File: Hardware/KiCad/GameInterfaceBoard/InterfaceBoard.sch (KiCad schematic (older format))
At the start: 23 parts, among them J1 CONN_11LOCK, J2 CONN_07LOCK

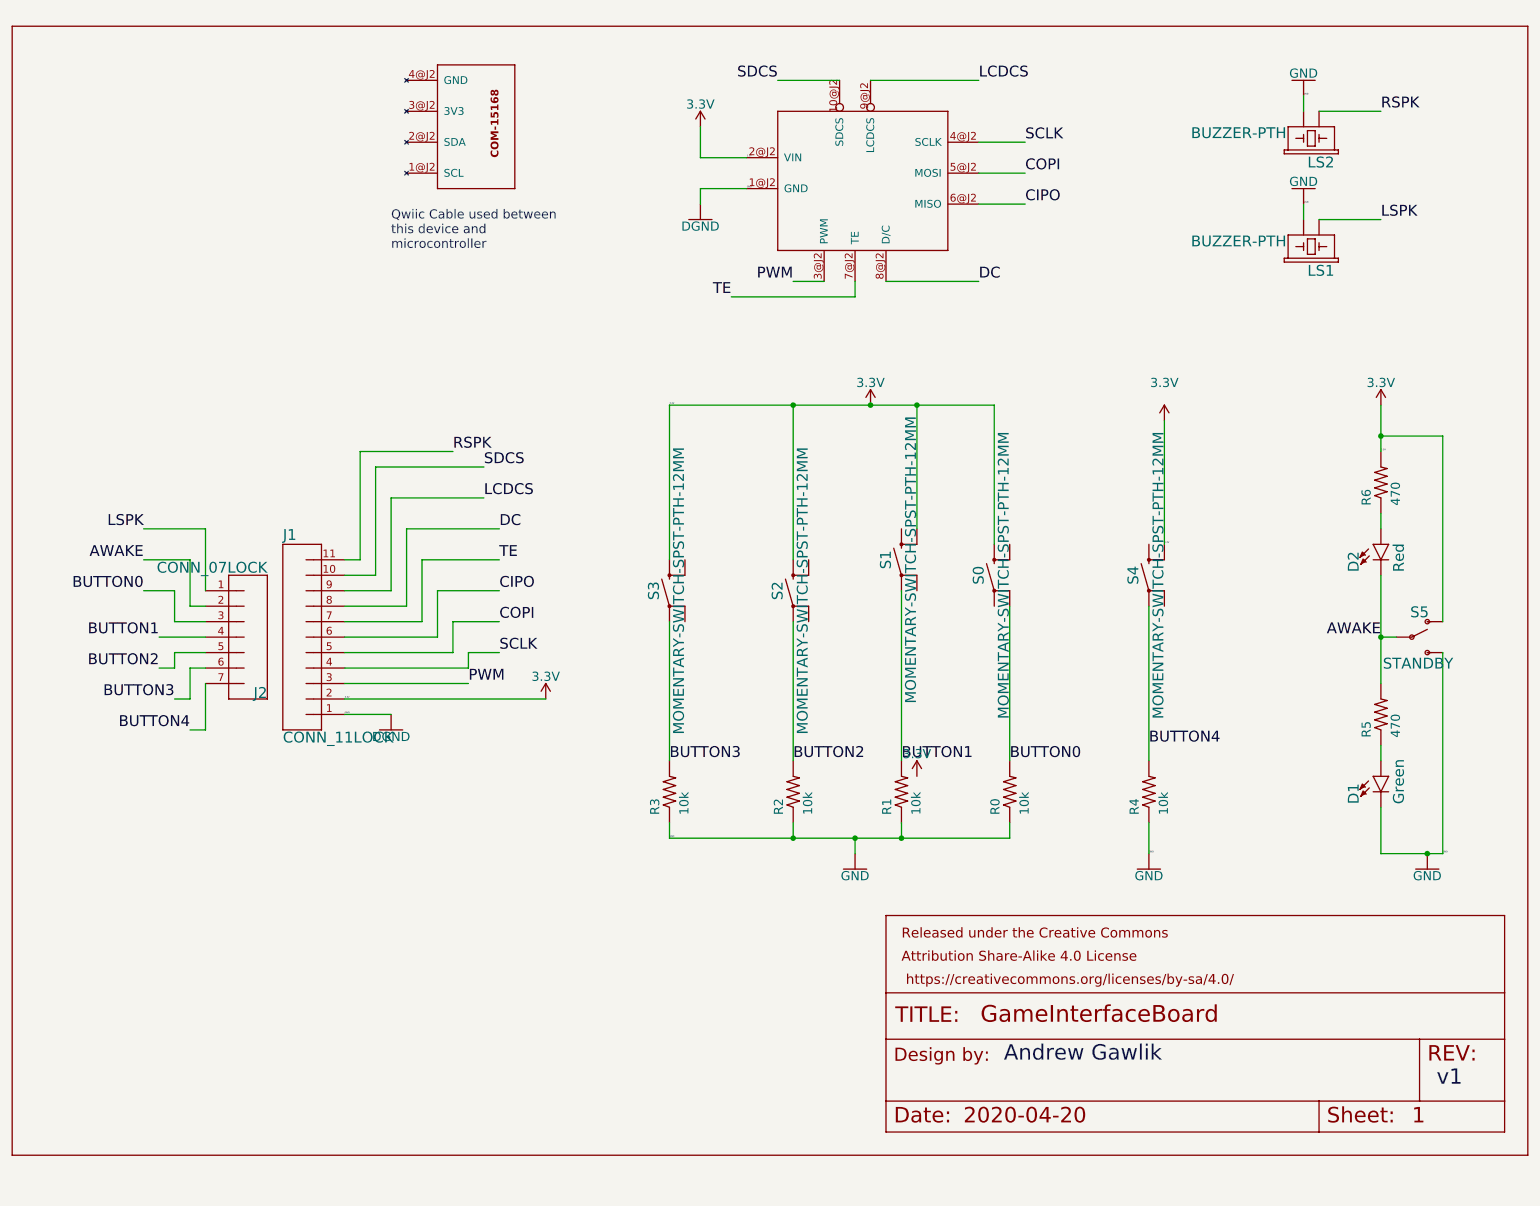
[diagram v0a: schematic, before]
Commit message: Added drill holes for issue #2
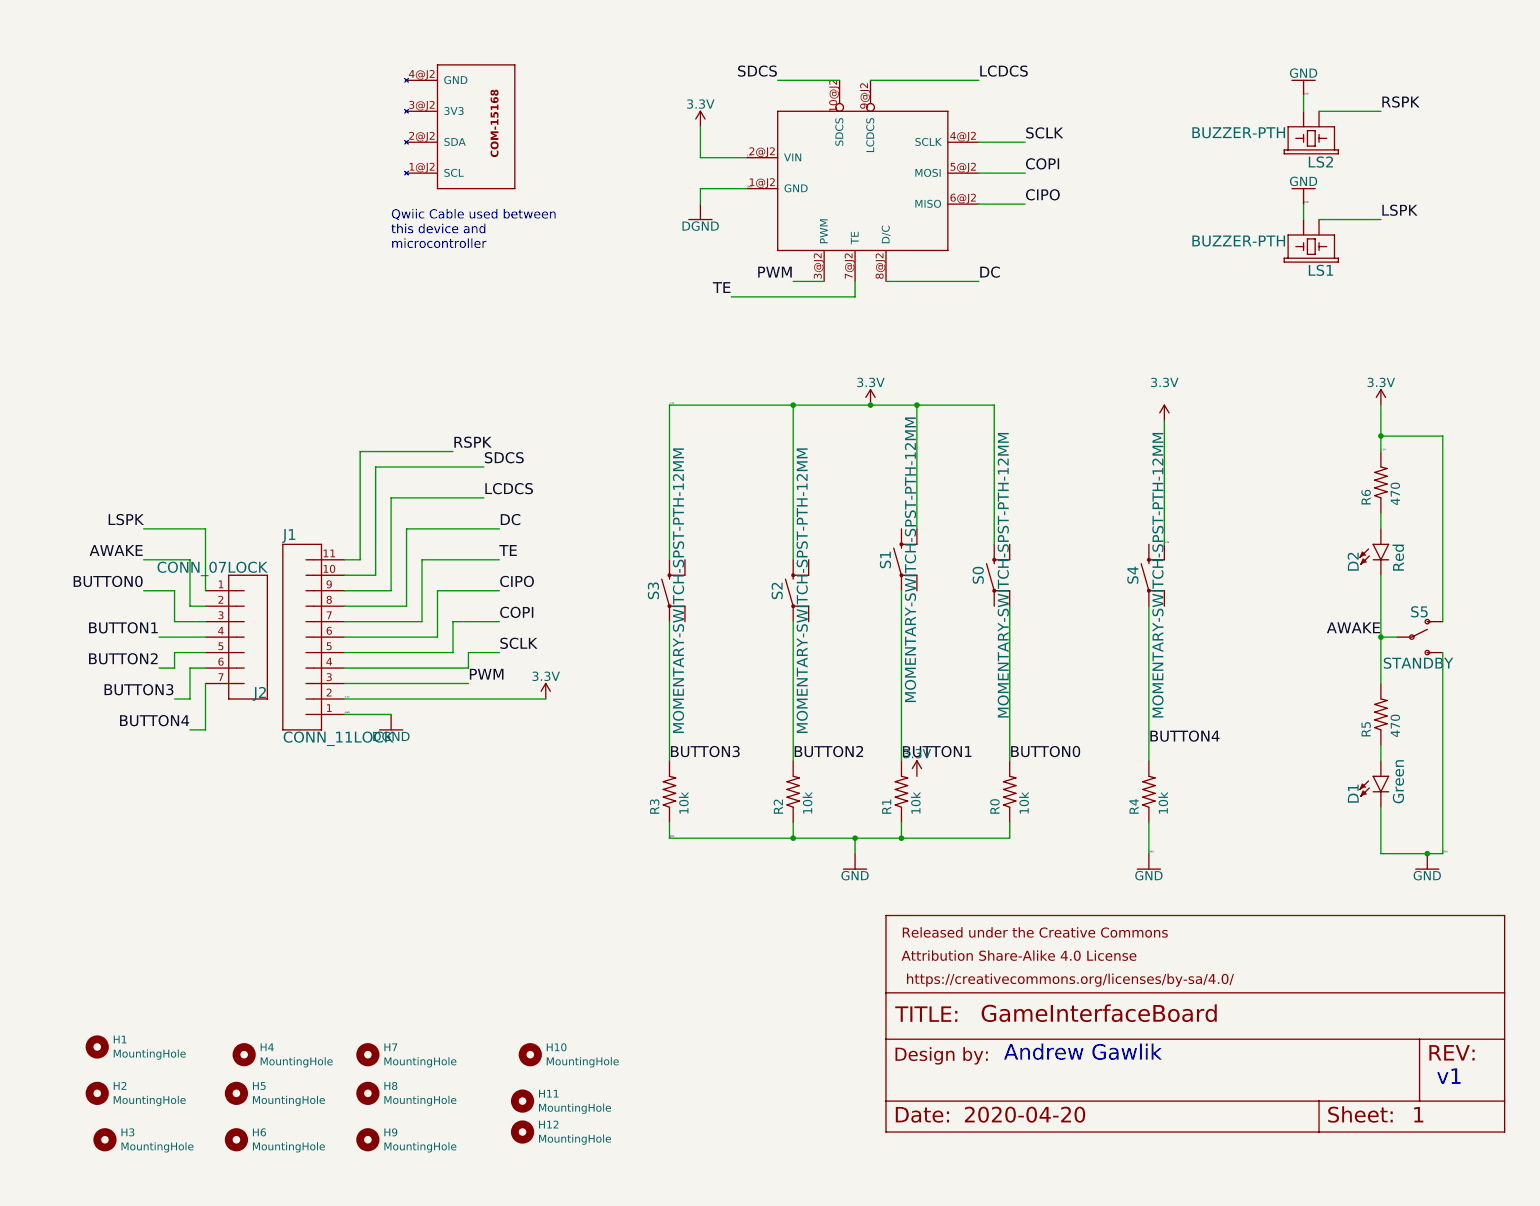
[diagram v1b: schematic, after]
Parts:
- removed FRAME2: FRAME-LETTER, InterfaceBoard:CREATIVE_COMMONS, symbol InterfaceBoard-eagle-import:FRAME-LETTER
- added H1, H10, H11, H12, H2, H3, H4, H5, H6, H7, H8, H9: MountingHole, MountingHole_3mm, symbol Mechanical:MountingHole
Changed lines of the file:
@@
 Text Notes 3700 2300 0    59   ~ 0
 Qwiic Cable used between\nthis device and\nmicrocontroller
-$Comp
-L InterfaceBoard-eagle-import:FRAME-LETTER FRAME2
-U 1 1 608402A7
-P 1250 8150
-F 0 "FRAME2" H 1250 8150 50  0001 C CNN
-F 1 "FRAME-LETTER" H 1250 8150 50  0001 C CNN
-F 2 "InterfaceBoard:CREATIVE_COMMONS" H 1250 8150 50  0001 C CNN
-F 3 "" H 1250 8150 50  0001 C CNN
-	1    1250 8150
-	1    0    0    -1
-$EndComp
 $Bitmap
 Pos 10450 6850
@@
 EndData
 $EndBitmap
+$Comp
+L Mechanical:MountingHole H4
+U 1 1 60808813
+P 2750 7500
+F 0 "H4" H 2850 7546 50  0000 L CNN
+F 1 "MountingHole" H 2850 7455 50  0000 L CNN
+F 2 "MountingHole_3mm" H 2750 7500 50  0001 C CNN
+F 3 "~" H 2750 7500 50  0001 C CNN
+	1    2750 7500
+	1    0    0    -1
+$EndComp
+$Comp
+L Mechanical:MountingHole H1
+U 1 1 6080D86C
+P 1800 7450
+F 0 "H1" H 1900 7496 50  0000 L CNN
+F 1 "MountingHole" H 1900 7405 50  0000 L CNN
+F 2 "MountingHole_3mm" H 1800 7450 50  0001 C CNN
+F 3 "~" H 1800 7450 50  0001 C CNN
+	1    1800 7450
+	1    0    0    -1
+$EndComp
+$Comp
+L Mechanical:MountingHole H7
+U 1 1 6081064F
+P 3550 7500
+F 0 "H7" H 3650 7546 50  0000 L CNN
+F 1 "MountingHole" H 3650 7455 50  0000 L CNN
+F 2 "MountingHole_3mm" H 3550 7500 50  0001 C CNN
+F 3 "~" H 3550 7500 50  0001 C CNN
+	1    3550 7500
+	1    0    0    -1
+$EndComp
+$Comp
+L Mechanical:MountingHole H8
+U 1 1 60810B66
+P 3550 7750
+F 0 "H8" H 3650 7796 50  0000 L CNN
+F 1 "MountingHole" H 3650 7705 50  0000 L CNN
+F 2 "MountingHole_3mm" H 3550 7750 50  0001 C CNN
+F 3 "~" H 3550 7750 50  0001 C CNN
+	1    3550 7750
+	1    0    0    -1
+$EndComp
+$Comp
+L Mechanical:MountingHole H3
+U 1 1 608113E1
+P 1850 8050
+F 0 "H3" H 1950 8096 50  0000 L CNN
+F 1 "MountingHole" H 1950 8005 50  0000 L CNN
+F 2 "MountingHole_3mm" H 1850 8050 50  0001 C CNN
+F 3 "~" H 1850 8050 50  0001 C CNN
+	1    1850 8050
+	1    0    0    -1
+$EndComp
+$Comp
+L Mechanical:MountingHole H6
+U 1 1 60811785
+P 2700 8050
+F 0 "H6" H 2800 8096 50  0000 L CNN
+F 1 "MountingHole" H 2800 8005 50  0000 L CNN
+F 2 "MountingHole_3mm" H 2700 8050 50  0001 C CNN
+F 3 "~" H 2700 8050 50  0001 C CNN
+	1    2700 8050
+	1    0    0    -1
+$EndComp
+$Comp
+L Mechanical:MountingHole H10
+U 1 1 60811E6B
+P 4600 7500
+F 0 "H10" H 4700 7546 50  0000 L CNN
+F 1 "MountingHole" H 4700 7455 50  0000 L CNN
+F 2 "MountingHole_3mm" H 4600 7500 50  0001 C CNN
+F 3 "~" H 4600 7500 50  0001 C CNN
+	1    4600 7500
+	1    0    0    -1
+$EndComp
+$Comp
+L Mechanical:MountingHole H12
+U 1 1 6081248E
+P 4550 8000
+F 0 "H12" H 4650 8046 50  0000 L CNN
+F 1 "MountingHole" H 4650 7955 50  0000 L CNN
+F 2 "MountingHole_3mm" H 4550 8000 50  0001 C CNN
+F 3 "~" H 4550 8000 50  0001 C CNN
+	1    4550 8000
+	1    0    0    -1
+$EndComp
+$Comp
+L Mechanical:MountingHole H2
+U 1 1 60812A9E
+P 1800 7750
+F 0 "H2" H 1900 7796 50  0000 L CNN
+F 1 "MountingHole" H 1900 7705 50  0000 L CNN
+F 2 "MountingHole_3mm" H 1800 7750 50  0001 C CNN
+F 3 "~" H 1800 7750 50  0001 C CNN
+	1    1800 7750
+	1    0    0    -1
+$EndComp
+$Comp
+L Mechanical:MountingHole H5
+U 1 1 60813FB8
+P 2700 7750
+F 0 "H5" H 2800 7796 50  0000 L CNN
+F 1 "MountingHole" H 2800 7705 50  0000 L CNN
+F 2 "MountingHole_3mm" H 2700 7750 50  0001 C CNN
+F 3 "~" H 2700 7750 50  0001 C CNN
+	1    2700 7750
+	1    0    0    -1
+$EndComp
+$Comp
+L Mechanical:MountingHole H9
+U 1 1 60814652
+P 3550 8050
+F 0 "H9" H 3650 8096 50  0000 L CNN
+F 1 "MountingHole" H 3650 8005 50  0000 L CNN
+F 2 "MountingHole_3mm" H 3550 8050 50  0001 C CNN
+F 3 "~" H 3550 8050 50  0001 C CNN
+	1    3550 8050
+	1    0    0    -1
+$EndComp
+$Comp
+L Mechanical:MountingHole H11
+U 1 1 60814DD4
+P 4550 7800
+F 0 "H11" H 4650 7846 50  0000 L CNN
+F 1 "MountingHole" H 4650 7755 50  0000 L CNN
+F 2 "MountingHole_3mm" H 4550 7800 50  0001 C CNN
+F 3 "~" H 4550 7800 50  0001 C CNN
+	1    4550 7800
+	1    0    0    -1
+$EndComp
 $EndSCHEMATC
